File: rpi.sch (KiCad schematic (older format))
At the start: 17 parts, among them J1 920-0135-01, Q1 DMMT5401, Q2 DMG2305UX, U1 CAT24C32

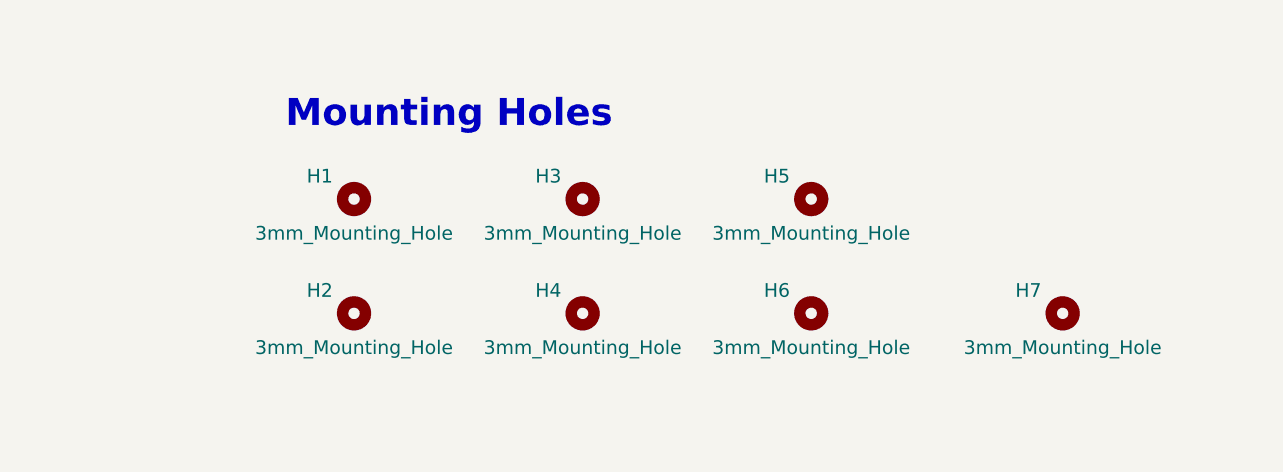
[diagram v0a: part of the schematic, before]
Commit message: Change mounting holes
Pi mounting holes: M2.5
Board mounting holes: M3

Added a mounting hole near the board center
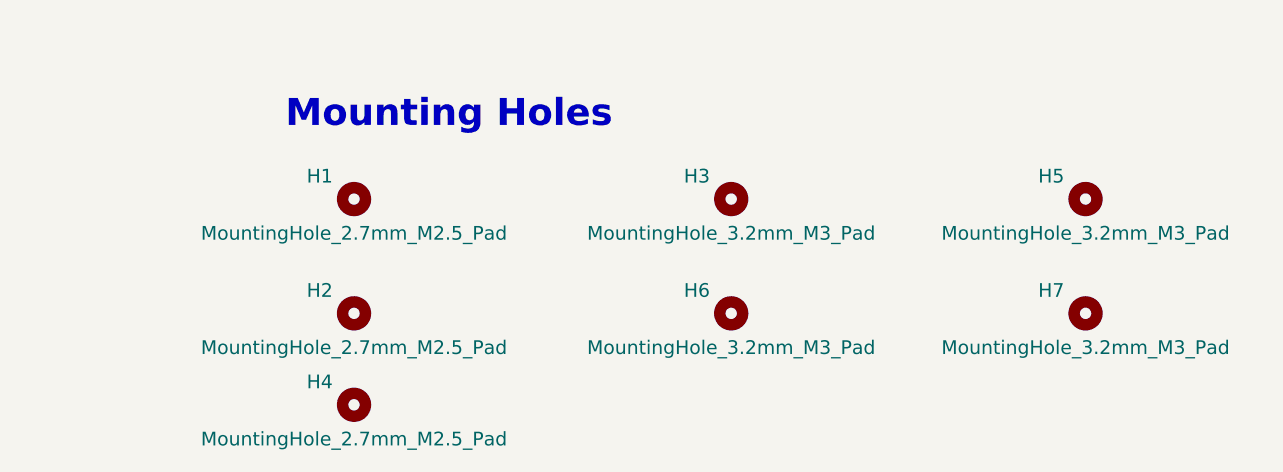
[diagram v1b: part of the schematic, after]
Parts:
- H1, H2, H4: value 3mm_Mounting_Hole -> MountingHole_2.7mm_M2.5_Pad; footprint heteromycin:MountingHole_3mm -> heteromycin:MountingHole_2.7mm_M2.5_Pad
- H3, H5, H6, H7: value 3mm_Mounting_Hole -> MountingHole_3.2mm_M3_Pad; footprint heteromycin:MountingHole_3mm -> heteromycin:MountingHole_3.2mm_M3_Pad
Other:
- moved on the sheet: H3, H4, H5, H6, H7
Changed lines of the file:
@@
 P 7050 4600
 F 0 "H1" H 6900 4700 60  0000 C CNN
-F 1 "3mm_Mounting_Hole" H 7050 4450 60  0000 C CNN
-F 2 "heteromycin:MountingHole_3mm" H 6950 4600 60  0001 C CNN
+F 1 "MountingHole_2.7mm_M2.5_Pad" H 7050 4450 60  0000 C CNN
+F 2 "heteromycin:MountingHole_2.7mm_M2.5_Pad" H 6950 4600 60  0001 C CNN
 F 3 "" H 6950 4600 60  0001 C CNN
 	1    7050 4600
@@
 P 7050 5100
 F 0 "H2" H 6900 5200 60  0000 C CNN
-F 1 "3mm_Mounting_Hole" H 7050 4950 60  0000 C CNN
-F 2 "heteromycin:MountingHole_3mm" H 6950 5100 60  0001 C CNN
+F 1 "MountingHole_2.7mm_M2.5_Pad" H 7050 4950 60  0000 C CNN
+F 2 "heteromycin:MountingHole_2.7mm_M2.5_Pad" H 6950 5100 60  0001 C CNN
 F 3 "" H 6950 5100 60  0001 C CNN
 	1    7050 5100
@@
 L Mechanical:MountingHole H4
 U 1 1 5BC4B23B
-P 8050 5100
-F 0 "H4" H 7900 5200 60  0000 C CNN
-F 1 "3mm_Mounting_Hole" H 8050 4950 60  0000 C CNN
-F 2 "heteromycin:MountingHole_3mm" H 7950 5100 60  0001 C CNN
-F 3 "" H 7950 5100 60  0001 C CNN
-	1    8050 5100
+P 7050 5500
+F 0 "H4" H 6900 5600 60  0000 C CNN
+F 1 "MountingHole_2.7mm_M2.5_Pad" H 7050 5350 60  0000 C CNN
+F 2 "heteromycin:MountingHole_2.7mm_M2.5_Pad" H 6950 5500 60  0001 C CNN
+F 3 "" H 6950 5500 60  0001 C CNN
+	1    7050 5500
 	1    0    0    -1
 $EndComp
@@
 L Mechanical:MountingHole H3
 U 1 1 5BC57D78
-P 8050 4600
-F 0 "H3" H 7900 4700 60  0000 C CNN
-F 1 "3mm_Mounting_Hole" H 8050 4450 60  0000 C CNN
-F 2 "heteromycin:MountingHole_3mm" H 7950 4600 60  0001 C CNN
-F 3 "" H 7950 4600 60  0001 C CNN
-	1    8050 4600
+P 8700 4600
+F 0 "H3" H 8550 4700 60  0000 C CNN
+F 1 "MountingHole_3.2mm_M3_Pad" H 8700 4450 60  0000 C CNN
+F 2 "heteromycin:MountingHole_3.2mm_M3_Pad" H 8600 4600 60  0001 C CNN
+F 3 "" H 8600 4600 60  0001 C CNN
+	1    8700 4600
 	1    0    0    -1
 $EndComp
@@
 L Mechanical:MountingHole H5
 U 1 1 5BC57D7F
-P 9050 4600
-F 0 "H5" H 8900 4700 60  0000 C CNN
-F 1 "3mm_Mounting_Hole" H 9050 4450 60  0000 C CNN
-F 2 "heteromycin:MountingHole_3mm" H 8950 4600 60  0001 C CNN
-F 3 "" H 8950 4600 60  0001 C CNN
-	1    9050 4600
+P 10250 4600
+F 0 "H5" H 10100 4700 60  0000 C CNN
+F 1 "MountingHole_3.2mm_M3_Pad" H 10250 4450 60  0000 C CNN
+F 2 "heteromycin:MountingHole_3.2mm_M3_Pad" H 10150 4600 60  0001 C CNN
+F 3 "" H 10150 4600 60  0001 C CNN
+	1    10250 4600
 	1    0    0    -1
 $EndComp
@@
 L Mechanical:MountingHole H6
 U 1 1 5BC57D86
-P 9050 5100
-F 0 "H6" H 8900 5200 60  0000 C CNN
-F 1 "3mm_Mounting_Hole" H 9050 4950 60  0000 C CNN
-F 2 "heteromycin:MountingHole_3mm" H 8950 5100 60  0001 C CNN
-F 3 "" H 8950 5100 60  0001 C CNN
-	1    9050 5100
+P 8700 5100
+F 0 "H6" H 8550 5200 60  0000 C CNN
+F 1 "MountingHole_3.2mm_M3_Pad" H 8700 4950 60  0000 C CNN
+F 2 "heteromycin:MountingHole_3.2mm_M3_Pad" H 8600 5100 60  0001 C CNN
+F 3 "" H 8600 5100 60  0001 C CNN
+	1    8700 5100
 	1    0    0    -1
 $EndComp
@@
 L Mechanical:MountingHole H7
 U 1 1 5BCFB1ED
-P 10150 5100
-F 0 "H7" H 10000 5200 60  0000 C CNN
-F 1 "3mm_Mounting_Hole" H 10150 4950 60  0000 C CNN
-F 2 "heteromycin:MountingHole_3mm" H 10050 5100 60  0001 C CNN
-F 3 "" H 10050 5100 60  0001 C CNN
-	1    10150 5100
-	1    0    0    -1
-$EndComp
+P 10250 5100
+F 0 "H7" H 10100 5200 60  0000 C CNN
+F 1 "MountingHole_3.2mm_M3_Pad" H 10250 4950 60  0000 C CNN
+F 2 "heteromycin:MountingHole_3.2mm_M3_Pad" H 10150 5100 60  0001 C CNN
+F 3 "" H 10150 5100 60  0001 C CNN
+	1    10250 5100
+	1    0    0    -1
+$EndComp

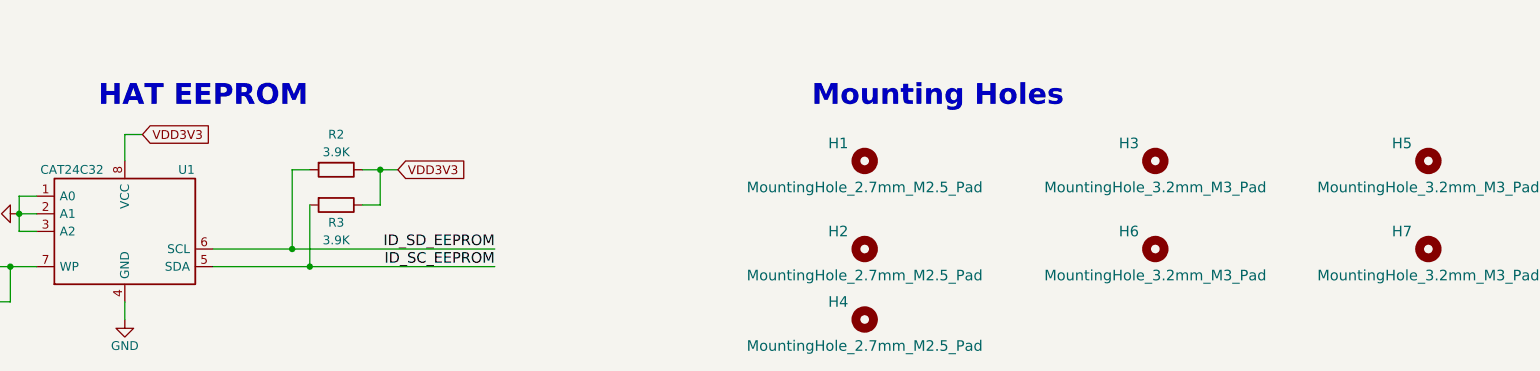
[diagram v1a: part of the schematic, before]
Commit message: Add bypass cap for I2C EEPROMs and redone some copper pour
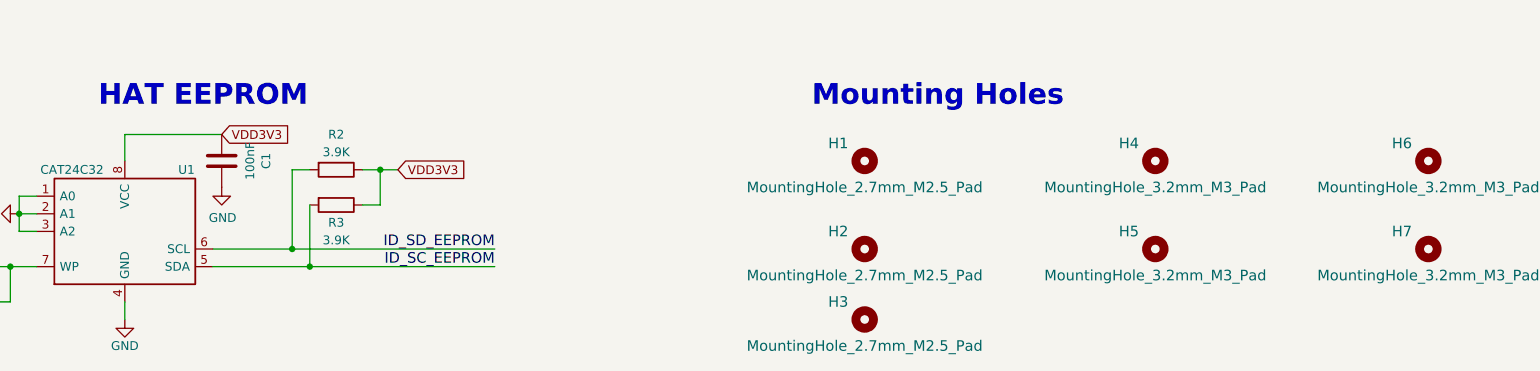
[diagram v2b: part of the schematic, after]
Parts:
- added C1: 100nF, Capacitor_SMD:C_0603_1608Metric, symbol Device:C
- renumbered H4 to H3, H3 to H4, H6 to H5, H5 to H6
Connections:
- net GND: now also C1.2
- net VDD3V3: now also C1.1
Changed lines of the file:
@@
 $EndComp
 $Comp
-L power:GND #PWR012
+L power:GND #PWR013
 U 1 1 5BC4B1B4
 P 7400 2650
-F 0 "#PWR012" H 7400 2400 50  0001 C CNN
+F 0 "#PWR013" H 7400 2400 50  0001 C CNN
 F 1 "GND" H 7400 2500 50  0000 C CNN
 F 2 "" H 7400 2650 50  0000 C CNN
@@
 $EndComp
 $Comp
-L power:GND #PWR013
+L power:GND #PWR014
 U 1 1 5BC4B1BA
 P 8200 2650
-F 0 "#PWR013" H 8200 2400 50  0001 C CNN
+F 0 "#PWR014" H 8200 2400 50  0001 C CNN
 F 1 "GND" H 8200 2500 50  0000 C CNN
 F 2 "" H 8200 2650 50  0000 C CNN
@@
 $EndComp
 $Comp
-L Mechanical:MountingHole H4
+L Mechanical:MountingHole H3
 U 1 1 5BC4B23B
 P 7050 5500
-F 0 "H4" H 6900 5600 60  0000 C CNN
+F 0 "H3" H 6900 5600 60  0000 C CNN
 F 1 "MountingHole_2.7mm_M2.5_Pad" H 7050 5350 60  0000 C CNN
 F 2 "heteromycin:MountingHole_2.7mm_M2.5_Pad" H 6950 5500 60  0001 C CNN
@@
 Text GLabel 1550 5400 0    50   Input ~ 0
 VDD3V3
-Text GLabel 2950 4450 2    50   Input ~ 0
+Text GLabel 3400 4450 2    50   Input ~ 0
 VDD3V3
 Wire Wire Line
@@
 Wire Wire Line
 	2850 4600 2850 4450
-Wire Wire Line
-	2850 4450 2950 4450
 Wire Wire Line
 	3350 5100 3800 5100
@@
 $EndComp
 $Comp
-L power:GND #PWR08
+L power:GND #PWR09
 U 1 1 5BC31A26
 P 3850 1700
-F 0 "#PWR08" H 3850 1450 50  0001 C CNN
+F 0 "#PWR09" H 3850 1450 50  0001 C CNN
 F 1 "GND" V 3855 1572 50  0000 R CNN
 F 2 "" H 3850 1700 50  0001 C CNN
@@
 $EndComp
 $Comp
-L power:GND #PWR09
+L power:GND #PWR010
 U 1 1 5BC343B5
 P 3850 2000
-F 0 "#PWR09" H 3850 1750 50  0001 C CNN
+F 0 "#PWR010" H 3850 1750 50  0001 C CNN
 F 1 "GND" V 3855 1872 50  0000 R CNN
 F 2 "" H 3850 2000 50  0001 C CNN
@@
 $EndComp
 $Comp
-L power:GND #PWR011
+L power:GND #PWR012
 U 1 1 5BC36329
 P 3850 2700
-F 0 "#PWR011" H 3850 2450 50  0001 C CNN
+F 0 "#PWR012" H 3850 2450 50  0001 C CNN
 F 1 "GND" V 3855 2572 50  0000 R CNN
 F 2 "" H 3850 2700 50  0001 C CNN
@@
 $EndComp
 $Comp
-L power:GND #PWR07
+L power:GND #PWR08
 U 1 1 5BC38606
 P 3850 1300
-F 0 "#PWR07" H 3850 1050 50  0001 C CNN
+F 0 "#PWR08" H 3850 1050 50  0001 C CNN
 F 1 "GND" V 3855 1172 50  0000 R CNN
 F 2 "" H 3850 1300 50  0001 C CNN
@@
 $EndComp
 $Comp
-L power:GND #PWR010
+L power:GND #PWR011
 U 1 1 5BC39EA4
 P 3850 2500
-F 0 "#PWR010" H 3850 2250 50  0001 C CNN
+F 0 "#PWR011" H 3850 2250 50  0001 C CNN
 F 1 "GND" V 3855 2372 50  0000 R CNN
 F 2 "" H 3850 2500 50  0001 C CNN
@@
 NoConn ~ 2650 1900
 $Comp
-L Mechanical:MountingHole H3
+L Mechanical:MountingHole H4
 U 1 1 5BC57D78
 P 8700 4600
-F 0 "H3" H 8550 4700 60  0000 C CNN
+F 0 "H4" H 8550 4700 60  0000 C CNN
 F 1 "MountingHole_3.2mm_M3_Pad" H 8700 4450 60  0000 C CNN
 F 2 "heteromycin:MountingHole_3.2mm_M3_Pad" H 8600 4600 60  0001 C CNN
@@
 $EndComp
 $Comp
-L Mechanical:MountingHole H5
+L Mechanical:MountingHole H6
 U 1 1 5BC57D7F
 P 10250 4600
-F 0 "H5" H 10100 4700 60  0000 C CNN
+F 0 "H6" H 10100 4700 60  0000 C CNN
 F 1 "MountingHole_3.2mm_M3_Pad" H 10250 4450 60  0000 C CNN
 F 2 "heteromycin:MountingHole_3.2mm_M3_Pad" H 10150 4600 60  0001 C CNN
@@
 $EndComp
 $Comp
-L Mechanical:MountingHole H6
+L Mechanical:MountingHole H5
 U 1 1 5BC57D86
 P 8700 5100
-F 0 "H6" H 8550 5200 60  0000 C CNN
+F 0 "H5" H 8550 5200 60  0000 C CNN
 F 1 "MountingHole_3.2mm_M3_Pad" H 8700 4950 60  0000 C CNN
 F 2 "heteromycin:MountingHole_3.2mm_M3_Pad" H 8600 5100 60  0001 C CNN
@@
 	1    0    0    -1
 $EndComp
+$Comp
+L Device:C C?
+U 1 1 5BD28BFC
+P 3400 4600
+AR Path="/5BC1C8A4/5BD28BFC" Ref="C?"  Part="1"
+AR Path="/5BC4AC32/5BD28BFC" Ref="C1"  Part="1"
+F 0 "C1" V 3652 4600 50  0000 C CNN
+F 1 "100nF" V 3561 4600 50  0000 C CNN
+F 2 "Capacitor_SMD:C_0603_1608Metric" H 3438 4450 50  0001 C CNN
+F 3 "~" H 3400 4600 50  0001 C CNN
+	1    3400 4600
+	1    0    0    -1
+$EndComp
+$Comp
+L power:GND #PWR?
+U 1 1 5BD28C03
+P 3400 4750
+AR Path="/5BC1C8A4/5BD28C03" Ref="#PWR?"  Part="1"
+AR Path="/5BC4AC32/5BD28C03" Ref="#PWR07"  Part="1"
+F 0 "#PWR07" H 3400 4500 50  0001 C CNN
+F 1 "GND" H 3405 4577 50  0000 C CNN
+F 2 "" H 3400 4750 50  0001 C CNN
+F 3 "" H 3400 4750 50  0001 C CNN
+	1    3400 4750
+	1    0    0    -1
+$EndComp
+Wire Wire Line
+	2850 4450 3400 4450
 $EndSCHEMATC

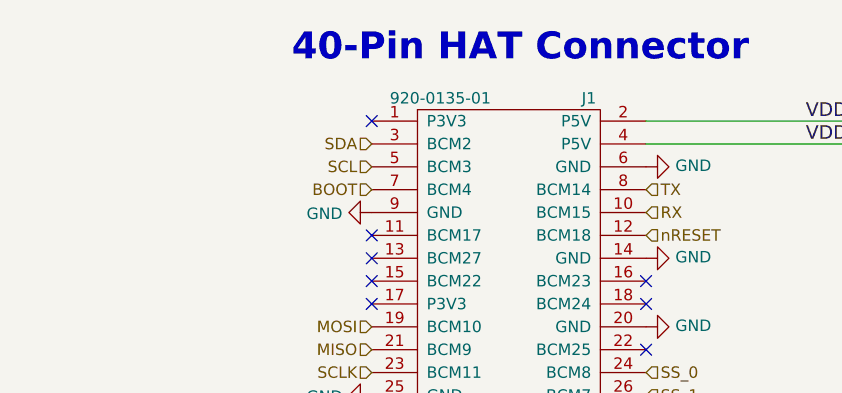
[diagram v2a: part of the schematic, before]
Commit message: Change PI connector to a cheaper one
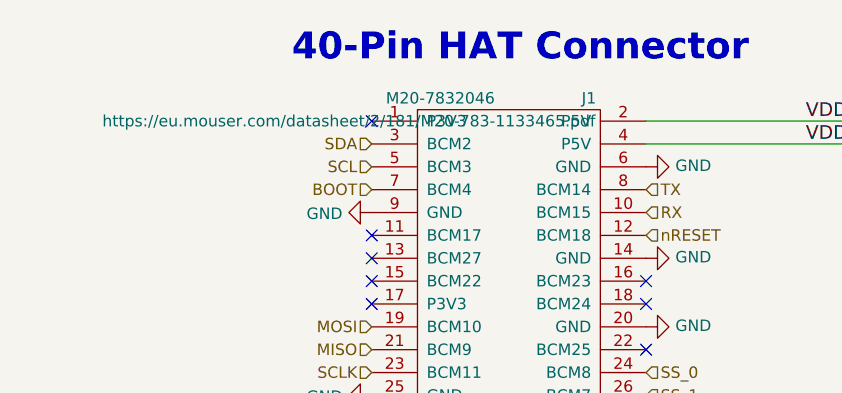
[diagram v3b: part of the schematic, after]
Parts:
- J1: value 920-0135-01 -> M20-7832046
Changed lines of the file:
@@
 P 3250 1100
 F 0 "J1" H 3600 1200 50  0000 C CNN
-F 1 "920-0135-01" H 2950 1200 50  0000 C CNN
+F 1 "M20-7832046" H 2950 1200 50  0000 C CNN
 F 2 "Connector_PinSocket_2.54mm:PinSocket_2x20_P2.54mm_Vertical" H 3250 1300 50  0001 C CNN
-F 3 "" H 2550 1100 50  0000 C CNN
+F 3 "https://eu.mouser.com/datasheet/2/181/M20-783-1133465.pdf" H 2550 1100 50  0000 C CNN
 	1    3250 1100
 	1    0    0    -1

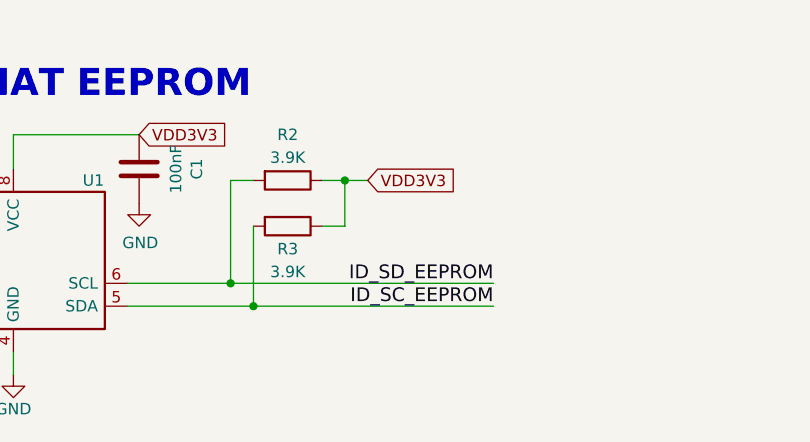
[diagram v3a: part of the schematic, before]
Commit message: Switched EEPROM I2C traces for the RPI
SDA and SCL were switched. Also some formatting for the
EEPROM settings.txt.
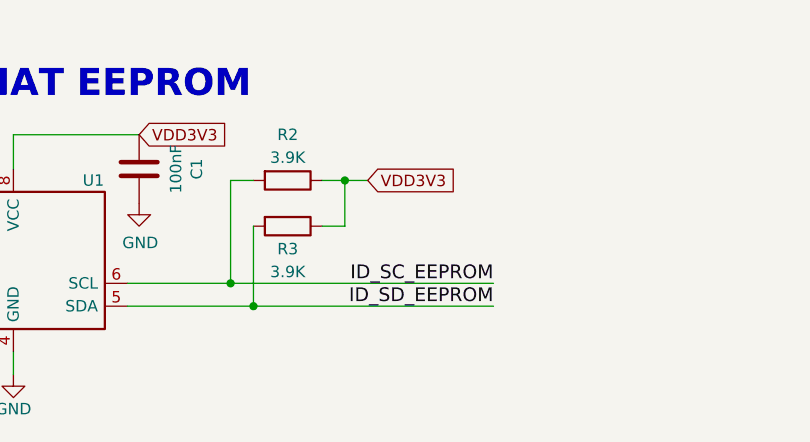
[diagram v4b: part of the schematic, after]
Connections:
- net ID_SC_EEPROM: now also R2.2, U1.6 (SCL); no longer R3.2, U1.5 (SDA)
- net ID_SD_EEPROM: now also R3.2, U1.5 (SDA); no longer R2.2, U1.6 (SCL)
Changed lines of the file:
@@
 	0    1    1    0
 $EndComp
+Text Label 4950 5200 2    60   ~ 0
+ID_SD_EEPROM
 Text Label 4950 5100 2    60   ~ 0
-ID_SD_EEPROM
-Text Label 4950 5200 2    60   ~ 0
 ID_SC_EEPROM
 $Comp
